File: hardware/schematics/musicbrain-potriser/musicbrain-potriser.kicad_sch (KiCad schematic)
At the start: 12 parts, among them J1 BUS, J2 NAAR POT8-FRONT, U1 MCP3208

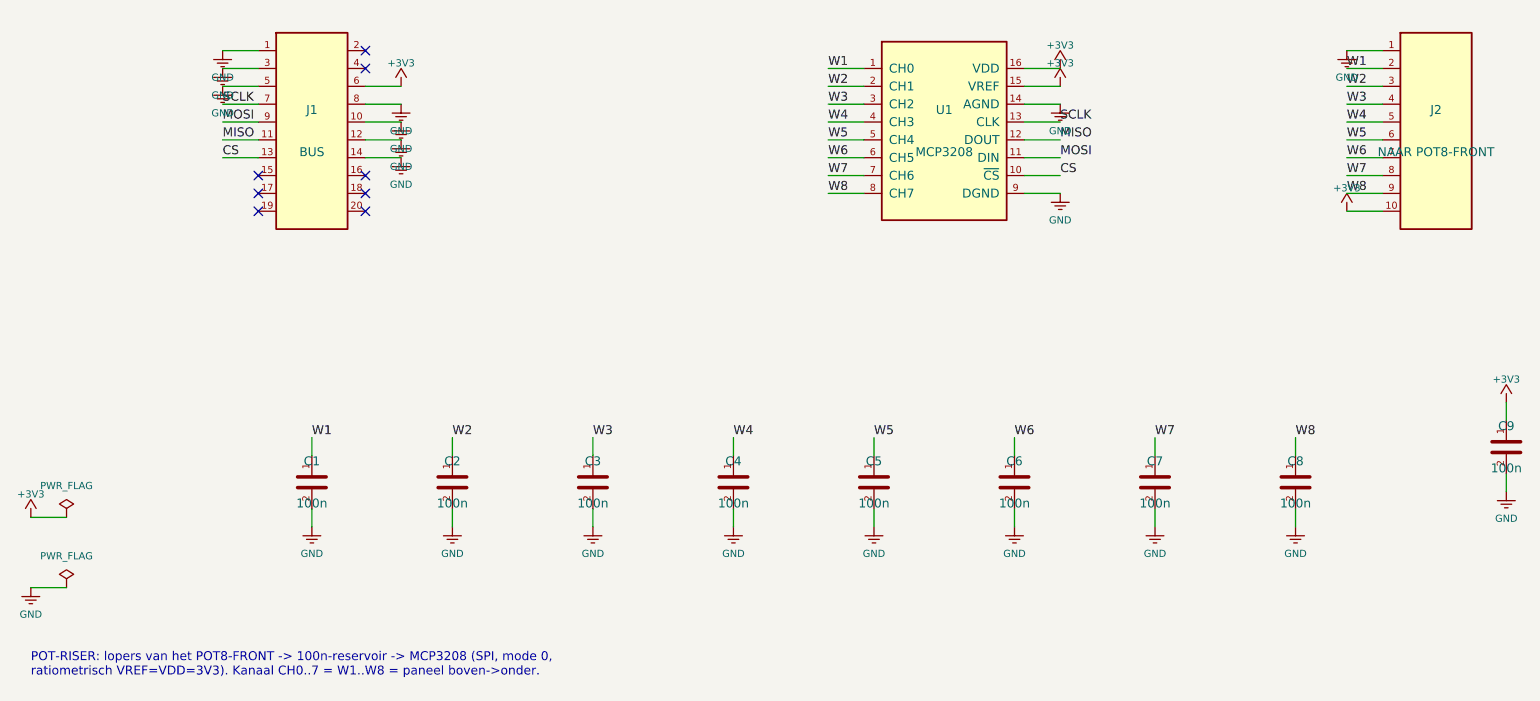
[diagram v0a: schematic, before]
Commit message: Gen 2 stap 3b/3c: riser + potriser rev 2.0 (2x12, H=50) DRC 0/0
riser: 40x50, hele 2x12-bus 1-op-1 omhoog incl. de audio-lijnen ->
ontwikkelbord voor een gedelegeerde Teensy/FPGA. x-matching schaalt mee:
J2-pin q draagt slotfunctie (24-q) oneven / (26-q) even.

potriser: 28x80 -> 80x50, J1 2x12; koper via freerouting i.p.v. handlanen
(1 unrouted -> snap_stubs dichtte 'm). Front-contract 1x10 ongewijzigd.

Meetvondst: de connector-bodies hangen bewust OVER de bordrand (zo mateert
de kaart met de socket eronder) -- dus de vrije kernband bij H=50 is 33,3 mm,
niet 18,8 zoals ik eerst schatte. Daarmee komt elke kaart op 80x50 uit op
5-16% dichtheid (adc8, de drukste: 15,6%) -- lager dan de huidige ~17% op
80 mm hoog. H=50 is dus ruim haalbaar voor alle kaarten.

Alle drie de risers: ERC 0 / netcheck OK / DRC 0/0.

Co-Authored-By: Claude Fable 5 <noreply@anthropic.com>
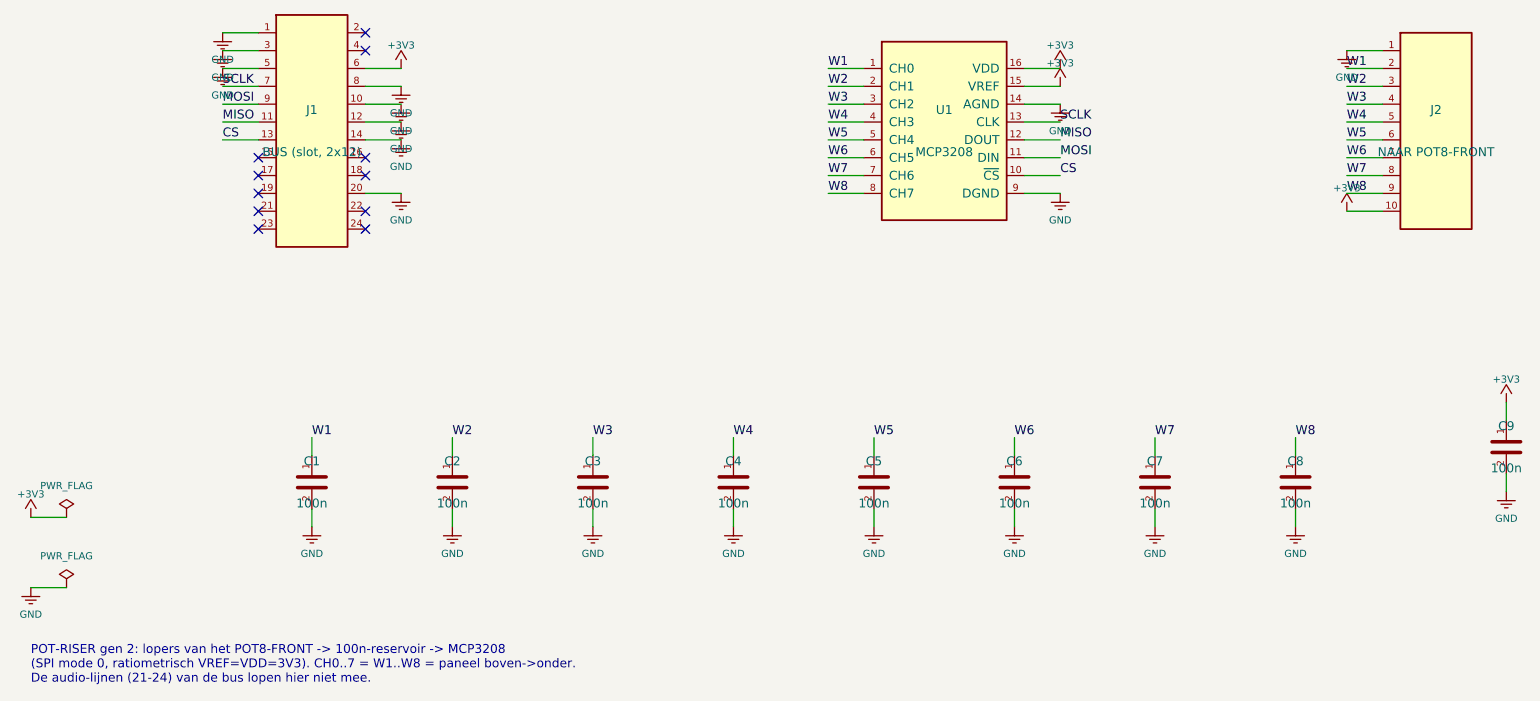
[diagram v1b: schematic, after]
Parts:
- removed C1: 100n, Capacitor_SMD:C_0805_2012Metric, symbol Device:C
- added C9: 100n, Capacitor_SMD:C_0805_2012Metric, symbol Device:C
- J1: value BUS -> BUS (slot, 2x12); footprint Connector_PinHeader_2.54mm:PinHeader_2x10_P2.54mm_Horizontal -> Connector_PinHeader_2.54mm:PinHeader_2x12_P2.54mm_Horizontal; symbol Custom:Conn_02x10 -> Custom:Conn_02x12
- renumbered C2 to C1, C3 to C2, C4 to C3, C5 to C4, C6 to C5, C7 to C6, C8 to C7, C9 to C8
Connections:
- net +3V3: now also C9.1; no longer C8.1
- net GND: now also J1.20 (Pin_20), C9.2
- net W1: now also C1.1
- net W2: now also C2.1; no longer C1.1
- net W3: now also C3.1; no longer C2.1
- net W4: now also C4.1; no longer C3.1
- net W5: now also C5.1; no longer C4.1
- net W6: now also C6.1; no longer C5.1
- net W7: now also C7.1; no longer C6.1
- net W8: now also C8.1; no longer C7.1
- no-connect marks 8 -> 11
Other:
- note added: "POT-RISER gen 2: lopers van het POT8-FRONT -> 100n-reservoir -> MCP3208 (SPI mode 0, ratiometrisch VREF=VDD=3V3). CH0..7 = W1..W8 = paneel boven->onder. De audio-lijnen (21-24) van de bus lopen hier niet mee."
- note removed: "POT-RISER: lopers van het POT8-FRONT -> 100n-reservoir -> MCP3208 (SPI, mode 0, ratiometrisch VREF=VDD=3V3). Kanaal CH0..7 = W1..W8 = paneel boven->onder."
- moved on the sheet: C1, C2, C3, C4, C5, C6, C7, C8
